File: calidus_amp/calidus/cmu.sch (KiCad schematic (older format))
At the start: 19 parts

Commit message: Daily update
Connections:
- net +pdvs: now also U?.20 (Vdd)
- net uart_rx: now also U?.18 (RC7); no longer U?.17 (RC6)
- net uart_tx: now also U?.17 (RC6); no longer U?.18 (RC7)
- net icsprst: now reaches R?.2, U?.1 (RE3/~MCLR~)
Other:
- note added: "The "pi_key_power" is tied on Vdd to \nsignal the FW boot to take instant \non action."
- note added: "pc_i2c_scl"
- note added: "pc_i2c_sda"
- note added: "pc_uart_rx"
- note added: "pc_uart_tx"
- note added: "pi_det_ac_power"
- note added: "pi_det_overload"
- note added: "pi_det_signal"
- note added: "pi_key_mute"
- note added: "pi_key_power"
- note added: "po_ctrl_enable"
- note added: "po_ctrl_mute"
- note added: "po_ctrl_pbypass"
- note added: "po_ctrl_power"
- note added: "po_ind_overload"
- note added: "po_ind_power_a"
- note added: "po_status"
- note removed: "The key "power" is tied on Vdd to \nsignal the FW boot to take instant \non action."
- moved on the sheet: D?, Q?, R?, U?

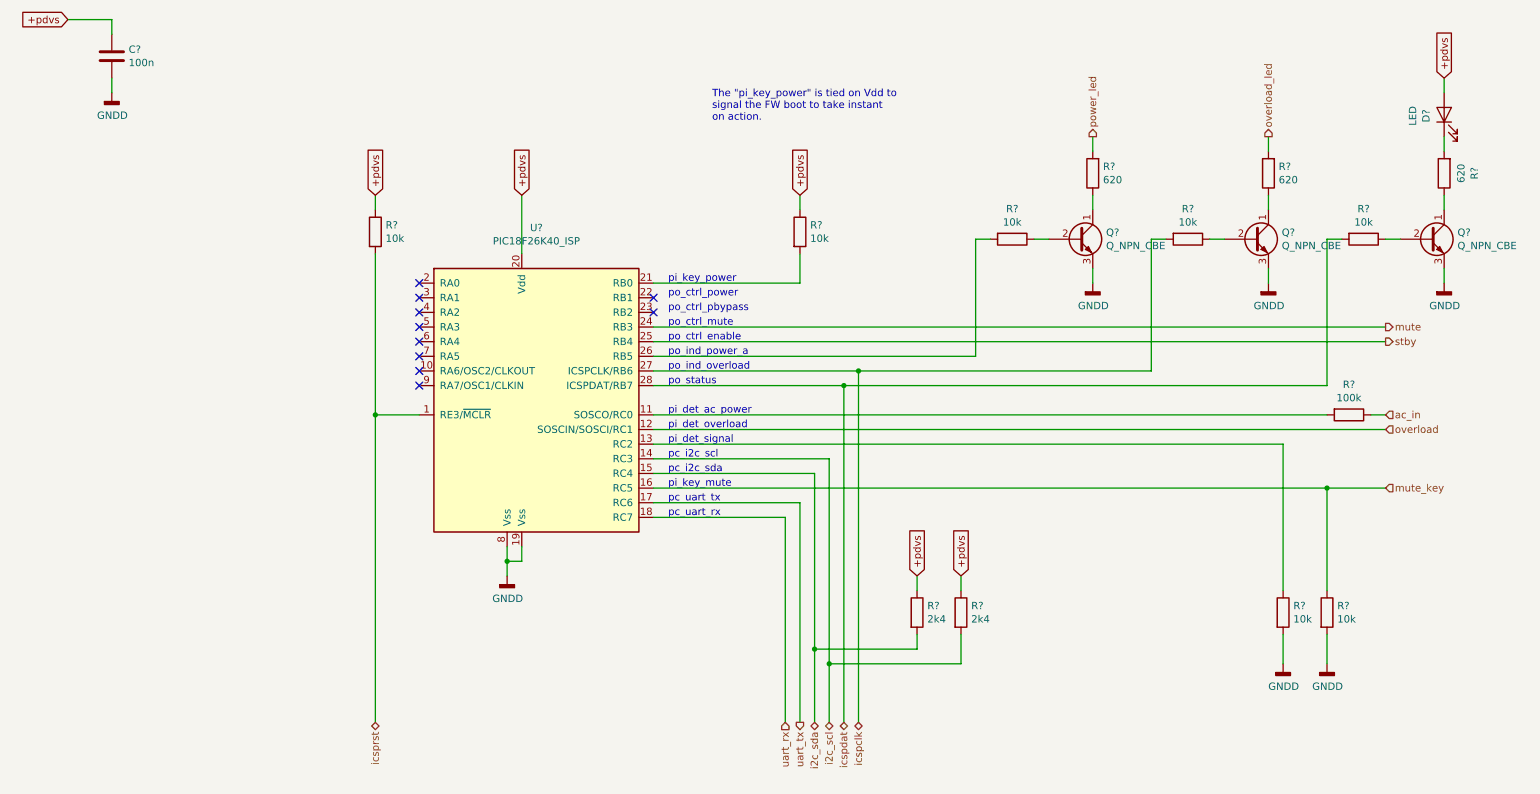
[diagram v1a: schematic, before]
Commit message: Updated component designators and finished CMU
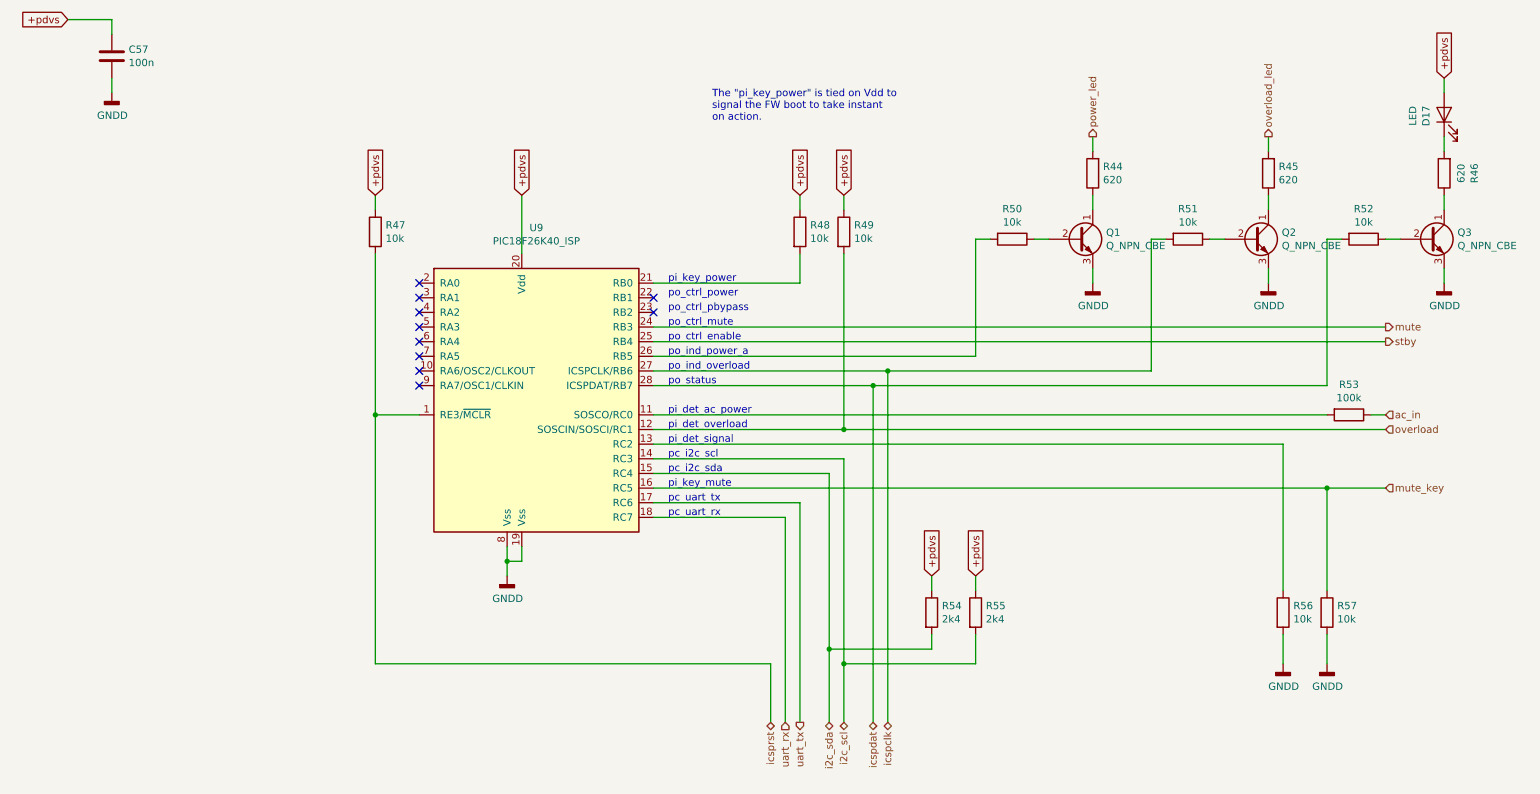
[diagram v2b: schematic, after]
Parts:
- added R49: 10k, symbol Device:R
- D17: renamed from D?; footprint (none) -> LED_THT:LED_D3.0mm
- U9: renamed from U?; footprint Package_SO:SSOP-28_5.3x10.2mm_P0.65mm -> Package_DIP:DIP-28_W7.62mm_LongPads
- gave numbers to parts that had none: 17
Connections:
- net +pdvs: now also R49.1
- net overload: now also R49.2
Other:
- moved on the sheet: R54, R55

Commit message: WIP: Updated footprints
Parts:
- removed R45, R46: 620, symbol Device:R
- removed R48, R49, R50, R51, R52, R56, R57: 10k, symbol Device:R
- removed R55: 2k4, symbol Device:R
- added C?: 10u, Capacitor_THT:CP_Radial_D5.0mm_P2.00mm, symbol Device:CP
- added R? (x7): 10k, Resistor_THT:R_Axial_DIN0204_L3.6mm_D1.6mm_P5.08mm_Horizontal, symbol Device:R
- added R?: 2k4, Resistor_THT:R_Axial_DIN0204_L3.6mm_D1.6mm_P5.08mm_Horizontal, symbol Device:R
- added R? (x2): 620, Resistor_THT:R_Axial_DIN0204_L3.6mm_D1.6mm_P5.08mm_Horizontal, symbol Device:R
- R44: footprint (none) -> Resistor_THT:R_Axial_DIN0204_L3.6mm_D1.6mm_P5.08mm_Horizontal; Manufacturer (none) -> Multicomp:MF12 620R; Power (none) -> 1/8; Supplier1 (none) -> Farnell:9343407; Type (none) -> C
- R47: footprint (none) -> Resistor_THT:R_Axial_DIN0204_L3.6mm_D1.6mm_P5.08mm_Horizontal; Manufacturer (none) -> Multicomp:MF12 10K; Power (none) -> 1/8; Supplier1 (none) -> Farnell:9342419; Type (none) -> C
- R54: footprint (none) -> Resistor_THT:R_Axial_DIN0204_L3.6mm_D1.6mm_P5.08mm_Horizontal; Manufacturer (none) -> Multicomp:MF12 2K4; Power (none) -> 1/8; Supplier1 (none) -> Farnell:9342893; Type (none) -> C
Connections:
- net +pdvs: now also C?.1, R?.1, R?.1, R?.1
- net GNDD: now also C?.2, R?.2, R?.2
- net i2c_scl: now also R?.2
- net icspclk: now also R?.2
- net icspdat: now also R?.2
- net mute_key: now also R?.1
- net overload: now also R?.2
- net overload_led: now also R?.2
- net at Q1.2 (B): now also R?.1
- net at U9.26 (RB5): now also R?.2
- net at Q2.1 (C): now also R?.1
- net at Q2.2 (B): now also R?.1
- net at Q3.1 (C): now also R?.1
- net at D17.1 (K): now also R?.2
- net at Q3.2 (B): now also R?.1
- net at U9.13 (RC2): now also R?.1
- net at U9.21 (RB0): now also R?.2

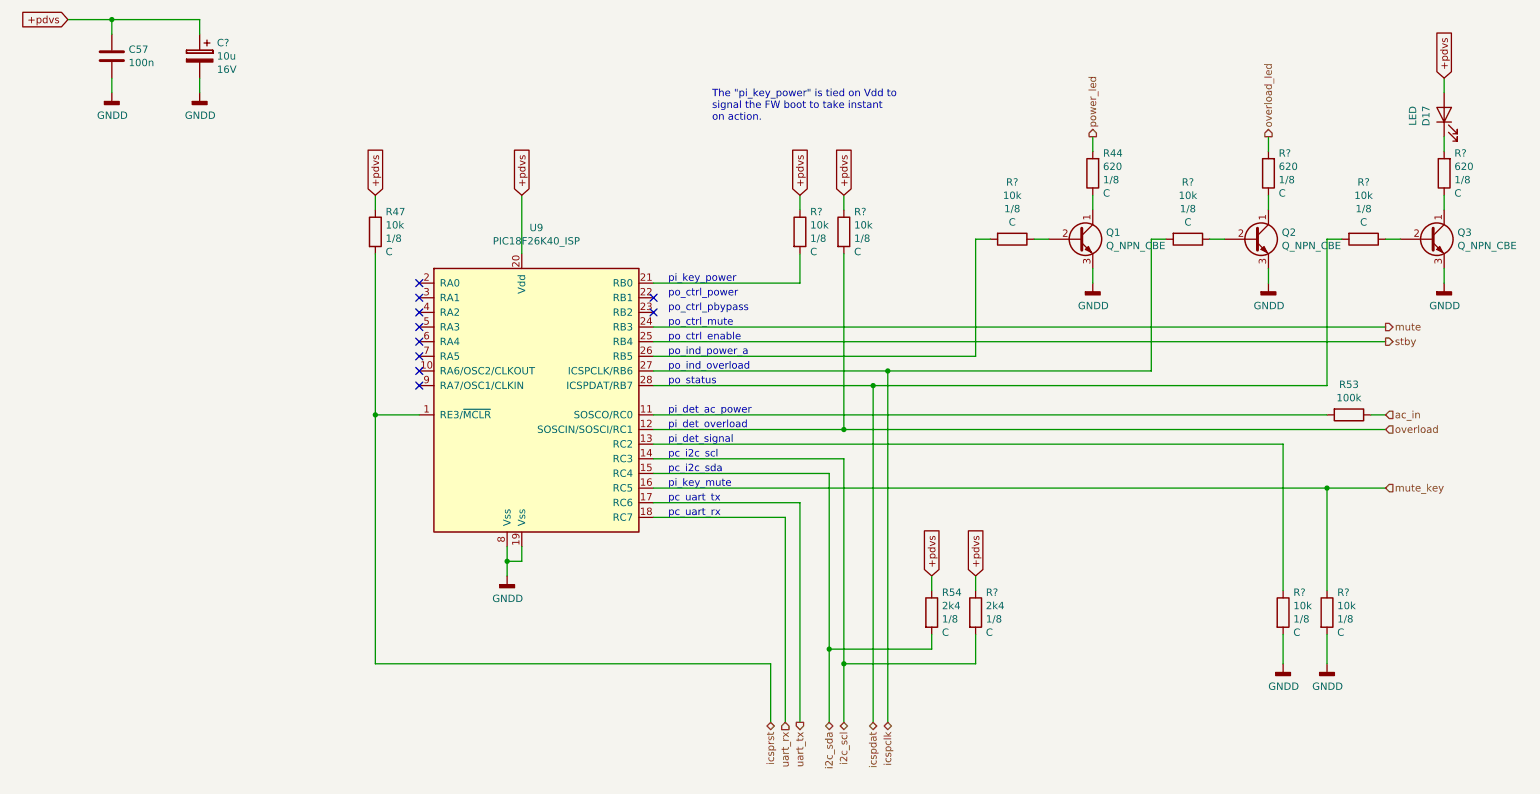
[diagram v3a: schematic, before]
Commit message: WIP: component footprint assignment.
Signed-off-by: Nenad Radulovic <nenad.b.radulovic@gmail.com>
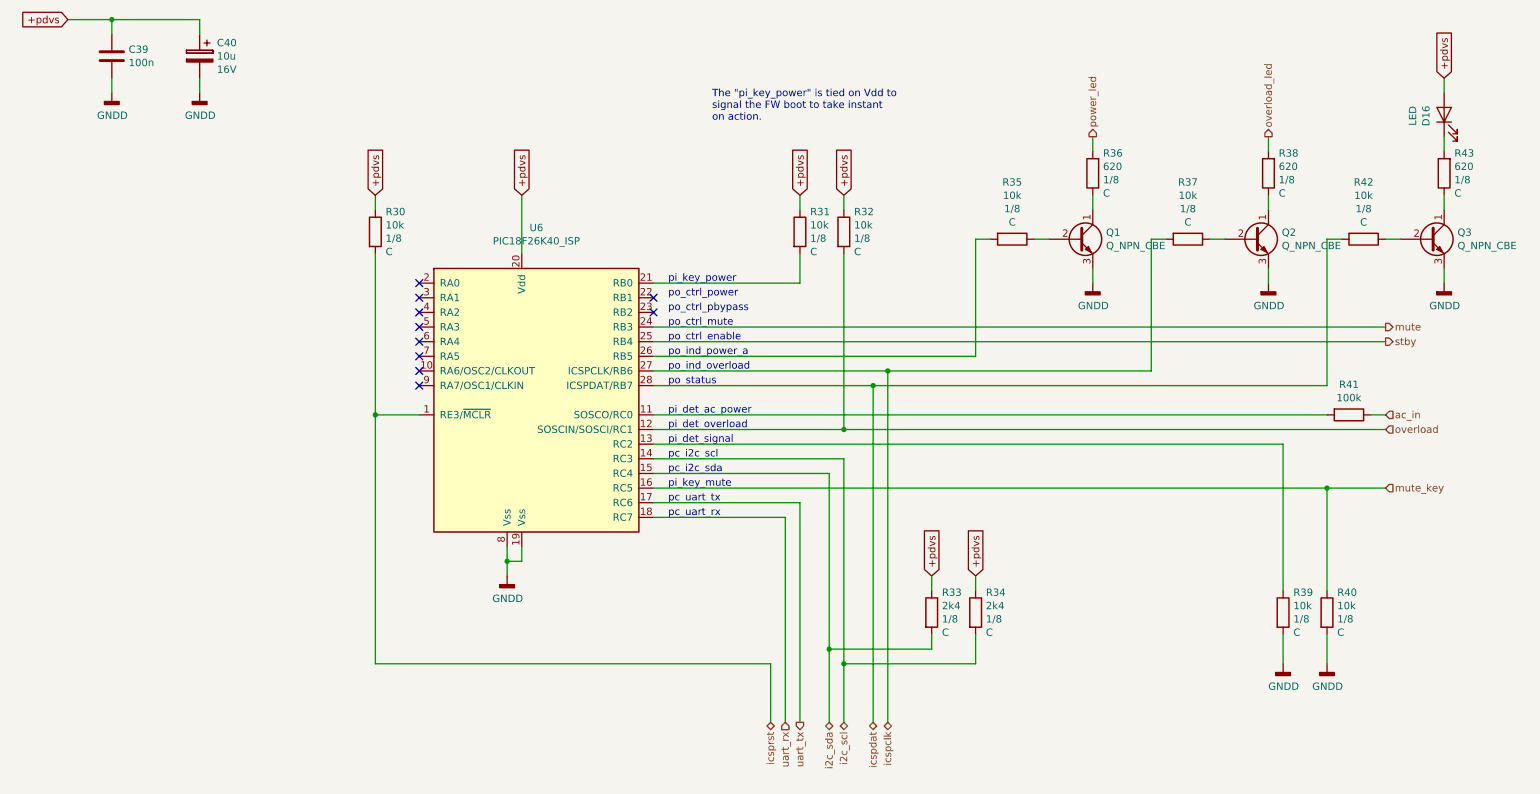
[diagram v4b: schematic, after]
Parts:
- C39: renamed from C57; footprint (none) -> Capacitor_THT:C_Rect_L7.0mm_W2.5mm_P5.00mm
- Q1, Q2, Q3: footprint (none) -> Package_TO_SOT_THT:TO-92_HandSolder
- R41: renamed from R53; footprint (none) -> Resistor_THT:R_Axial_DIN0207_L6.3mm_D2.5mm_P7.62mm_Horizontal
- gave numbers to parts that had none: 11
- renumbered D17 to D16, R47 to R30, R54 to R33, R44 to R36, U9 to U6
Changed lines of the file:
@@
 $Descr A4 11693 8268
 encoding utf-8
-Sheet 5 5
+Sheet 5 4
 Title ""
 Date ""
@@
 $EndDescr
 $Comp
-L power:GNDD #PWR036
+L power:GNDD #PWR031
 U 1 1 5C444574
 P 4200 5200
-F 0 "#PWR036" H 4200 4950 50  0001 C CNN
+F 0 "#PWR031" H 4200 4950 50  0001 C CNN
 F 1 "GNDD" H 4204 5045 50  0000 C CNN
 F 2 "" H 4200 5200 50  0001 C CNN
@@
 	1500 1400 1500 1500
 $Comp
-L power:GNDD #PWR032
+L power:GNDD #PWR029
 U 1 1 5C444792
 P 1500 1900
-F 0 "#PWR032" H 1500 1650 50  0001 C CNN
+F 0 "#PWR029" H 1500 1650 50  0001 C CNN
 F 1 "GNDD" H 1504 1745 50  0000 C CNN
 F 2 "" H 1500 1900 50  0001 C CNN
@@
 $EndComp
 $Comp
-L Device:C C57
+L Device:C C39
 U 1 1 5C46D3BF
 P 1500 1650
-F 0 "C57" H 1615 1696 50  0000 L CNN
+F 0 "C39" H 1615 1696 50  0000 L CNN
 F 1 "100n" H 1615 1605 50  0000 L CNN
-F 2 "" H 1538 1500 50  0001 C CNN
+F 2 "Capacitor_THT:C_Rect_L7.0mm_W2.5mm_P5.00mm" H 1538 1500 50  0001 C CNN
 F 3 "~" H 1500 1650 50  0001 C CNN
 	1    1500 1650
@@
 	1500 1800 1500 1900
 $Comp
-L pic18f26k40_isp:PIC18F26K40_ISP U9
+L pic18f26k40_isp:PIC18F26K40_ISP U6
 U 1 1 5C470457
 P 4400 4000
-F 0 "U9" H 4400 5178 50  0000 C CNN
+F 0 "U6" H 4400 5178 50  0000 C CNN
 F 1 "PIC18F26K40_ISP" H 4400 5087 50  0000 C CNN
 F 2 "Package_DIP:DIP-28_W7.62mm_LongPads" H 3900 3500 50  0001 C CNN
@@
 NoConn ~ 5200 3300
 $Comp
-L Device:R R44
+L Device:R R36
 U 1 1 5C48301D
 P 8200 2450
-F 0 "R44" H 8130 2313 50  0000 R CNN
+F 0 "R36" H 8130 2313 50  0000 R CNN
 F 1 "620" H 8130 2404 50  0000 R CNN
 F 2 "Resistor_THT:R_Axial_DIN0204_L3.6mm_D1.6mm_P5.08mm_Horizontal" V 8130 2450 50  0001 C CNN
@@
 overload_led
 $Comp
-L Device:LED D17
+L Device:LED D16
 U 1 1 5C4834BB
 P 10600 2050
-F 0 "D17" H 10592 2173 50  0000 C CNN
+F 0 "D16" H 10592 2173 50  0000 C CNN
 F 1 "LED" H 10592 2264 50  0000 C CNN
 F 2 "LED_THT:LED_D3.0mm" H 10600 2050 50  0001 C CNN
@@
 $EndComp
 $Comp
-L power:GNDD #PWR033
+L power:GNDD #PWR032
 U 1 1 5C4835A2
 P 8200 3200
-F 0 "#PWR033" H 8200 2950 50  0001 C CNN
+F 0 "#PWR032" H 8200 2950 50  0001 C CNN
 F 1 "GNDD" H 8204 3045 50  0000 C CNN
 F 2 "" H 8200 3200 50  0001 C CNN
@@
 F 0 "Q1" H 8291 2946 50  0000 L CNN
 F 1 "Q_NPN_CBE" H 8291 2855 50  0000 L CNN
-F 2 "" H 8300 3000 50  0001 C CNN
+F 2 "Package_TO_SOT_THT:TO-92_HandSolder" H 8300 3000 50  0001 C CNN
 F 3 "~" H 8100 2900 50  0001 C CNN
 	1    8100 2900
@@
 F 0 "Q2" H 9491 2946 50  0000 L CNN
 F 1 "Q_NPN_CBE" H 9491 2855 50  0000 L CNN
-F 2 "" H 9500 3000 50  0001 C CNN
+F 2 "Package_TO_SOT_THT:TO-92_HandSolder" H 9500 3000 50  0001 C CNN
 F 3 "~" H 9300 2900 50  0001 C CNN
 	1    9300 2900
@@
 F 0 "Q3" H 10691 2946 50  0000 L CNN
 F 1 "Q_NPN_CBE" H 10691 2855 50  0000 L CNN
-F 2 "" H 10700 3000 50  0001 C CNN
+F 2 "Package_TO_SOT_THT:TO-92_HandSolder" H 10700 3000 50  0001 C CNN
 F 3 "~" H 10500 2900 50  0001 C CNN
 	1    10500 2900
@@
 	8200 3200 8200 3100
 $Comp
-L power:GNDD #PWR034
+L power:GNDD #PWR033
 U 1 1 5C46343D
 P 9400 3200
-F 0 "#PWR034" H 9400 2950 50  0001 C CNN
+F 0 "#PWR033" H 9400 2950 50  0001 C CNN
 F 1 "GNDD" H 9404 3045 50  0000 C CNN
 F 2 "" H 9400 3200 50  0001 C CNN
@@
 $EndComp
 $Comp
-L power:GNDD #PWR035
+L power:GNDD #PWR036
 U 1 1 5C463464
 P 10600 3200
-F 0 "#PWR035" H 10600 2950 50  0001 C CNN
+F 0 "#PWR036" H 10600 2950 50  0001 C CNN
 F 1 "GNDD" H 10604 3045 50  0000 C CNN
 F 2 "" H 10600 3200 50  0001 C CNN
@@
 	9800 2900 9900 2900
 $Comp
-L Device:R R47
+L Device:R R30
 U 1 1 5C4640C2
 P 3300 2850
-F 0 "R47" H 3370 2987 50  0000 L CNN
+F 0 "R30" H 3370 2987 50  0000 L CNN
 F 1 "10k" H 3370 2896 50  0000 L CNN
 F 2 "Resistor_THT:R_Axial_DIN0204_L3.6mm_D1.6mm_P5.08mm_Horizontal" V 3230 2850 50  0001 C CNN
@@
 	10200 4200 6500 4200
 $Comp
-L Device:R R53
+L Device:R R41
 U 1 1 5C466052
 P 9950 4100
-F 0 "R53" V 9743 4100 50  0000 C CNN
+F 0 "R41" V 9743 4100 50  0000 C CNN
 F 1 "100k" V 9834 4100 50  0000 C CNN
-F 2 "" V 9880 4100 50  0001 C CNN
+F 2 "Resistor_THT:R_Axial_DIN0207_L6.3mm_D2.5mm_P7.62mm_Horizontal" V 9880 4100 50  0001 C CNN
 F 3 "~" H 9950 4100 50  0001 C CNN
 	1    9950 4100
@@
 	6500 4400 5200 4400
 $Comp
-L power:GNDD #PWR037
+L power:GNDD #PWR034
 U 1 1 5C475E16
 P 9500 5800
-F 0 "#PWR037" H 9500 5550 50  0001 C CNN
+F 0 "#PWR034" H 9500 5550 50  0001 C CNN
 F 1 "GNDD" H 9504 5645 50  0000 C CNN
 F 2 "" H 9500 5800 50  0001 C CNN
@@
 $EndComp
 $Comp
-L power:GNDD #PWR038
+L power:GNDD #PWR035
 U 1 1 5C476CD2
 P 9800 5800
-F 0 "#PWR038" H 9800 5550 50  0001 C CNN
+F 0 "#PWR035" H 9800 5550 50  0001 C CNN
 F 1 "GNDD" H 9804 5645 50  0000 C CNN
 F 2 "" H 9800 5800 50  0001 C CNN
@@
 $EndComp
 $Comp
-L Device:R R54
+L Device:R R33
 U 1 1 5C477BD2
 P 7100 5450
-F 0 "R54" H 7170 5587 50  0000 L CNN
+F 0 "R33" H 7170 5587 50  0000 L CNN
 F 1 "2k4" H 7170 5496 50  0000 L CNN
 F 2 "Resistor_THT:R_Axial_DIN0204_L3.6mm_D1.6mm_P5.08mm_Horizontal" V 7030 5450 50  0001 C CNN
@@
 	6500 4200 5200 4200
 $Comp
-L Device:R R?
+L Device:R R31
 U 1 1 5C4C2301
 P 6200 2850
-F 0 "R?" H 6270 2987 50  0000 L CNN
+F 0 "R31" H 6270 2987 50  0000 L CNN
 F 1 "10k" H 6270 2896 50  0000 L CNN
 F 2 "Resistor_THT:R_Axial_DIN0204_L3.6mm_D1.6mm_P5.08mm_Horizontal" V 6130 2850 50  0001 C CNN
@@
 $EndComp
 $Comp
-L Device:R R?
+L Device:R R32
 U 1 1 5C4C234B
 P 6500 2850
-F 0 "R?" H 6570 2987 50  0000 L CNN
+F 0 "R32" H 6570 2987 50  0000 L CNN
 F 1 "10k" H 6570 2896 50  0000 L CNN
 F 2 "Resistor_THT:R_Axial_DIN0204_L3.6mm_D1.6mm_P5.08mm_Horizontal" V 6430 2850 50  0001 C CNN
@@
 $EndComp
 $Comp
-L Device:R R?
+L Device:R R39
 U 1 1 5C4C2657
 P 9500 5450
-F 0 "R?" H 9570 5587 50  0000 L CNN
+F 0 "R39" H 9570 5587 50  0000 L CNN
 F 1 "10k" H 9570 5496 50  0000 L CNN
 F 2 "Resistor_THT:R_Axial_DIN0204_L3.6mm_D1.6mm_P5.08mm_Horizontal" V 9430 5450 50  0001 C CNN
@@
 $EndComp
 $Comp
-L Device:R R?
+L Device:R R40
 U 1 1 5C4C26B7
 P 9800 5450
-F 0 "R?" H 9870 5587 50  0000 L CNN
+F 0 "R40" H 9870 5587 50  0000 L CNN
 F 1 "10k" H 9870 5496 50  0000 L CNN
 F 2 "Resistor_THT:R_Axial_DIN0204_L3.6mm_D1.6mm_P5.08mm_Horizontal" V 9730 5450 50  0001 C CNN
@@
 $EndComp
 $Comp
-L Device:R R?
+L Device:R R35
 U 1 1 5C4C2732
 P 7650 2900
-F 0 "R?" V 7261 2900 50  0000 C CNN
+F 0 "R35" V 7261 2900 50  0000 C CNN
 F 1 "10k" V 7352 2900 50  0000 C CNN
 F 2 "Resistor_THT:R_Axial_DIN0204_L3.6mm_D1.6mm_P5.08mm_Horizontal" V 7580 2900 50  0001 C CNN
@@
 $EndComp
 $Comp
-L Device:R R?
+L Device:R R37
 U 1 1 5C4C2878
 P 8850 2900
-F 0 "R?" V 8461 2900 50  0000 C CNN
+F 0 "R37" V 8461 2900 50  0000 C CNN
 F 1 "10k" V 8552 2900 50  0000 C CNN
 F 2 "Resistor_THT:R_Axial_DIN0204_L3.6mm_D1.6mm_P5.08mm_Horizontal" V 8780 2900 50  0001 C CNN
@@
 $EndComp
 $Comp
-L Device:R R?
+L Device:R R42
 U 1 1 5C4C28CE
 P 10050 2900
-F 0 "R?" V 9661 2900 50  0000 C CNN
+F 0 "R42" V 9661 2900 50  0000 C CNN
 F 1 "10k" V 9752 2900 50  0000 C CNN
 F 2 "Resistor_THT:R_Axial_DIN0204_L3.6mm_D1.6mm_P5.08mm_Horizontal" V 9980 2900 50  0001 C CNN
@@
 P 2100 1650
 AR Path="/5C37BC7C/5C4C9FCF" Ref="C?"  Part="1"
-AR Path="/5C43C4AB/5C4C9FCF" Ref="C?"  Part="1"
-F 0 "C?" H 1982 1741 50  0000 R CNN
+AR Path="/5C43C4AB/5C4C9FCF" Ref="C40"  Part="1"
+F 0 "C40" H 1982 1741 50  0000 R CNN
 F 1 "10u" H 1982 1650 50  0000 R CNN
 F 2 "Capacitor_THT:CP_Radial_D5.0mm_P2.00mm" H 2138 1500 50  0001 C CNN
@@
 $EndComp
 $Comp
-L power:GNDD #PWR?
+L power:GNDD #PWR030
 U 1 1 5C4CB7C3
 P 2100 1900
-F 0 "#PWR?" H 2100 1650 50  0001 C CNN
+F 0 "#PWR030" H 2100 1650 50  0001 C CNN
 F 1 "GNDD" H 2104 1745 50  0000 C CNN
 F 2 "" H 2100 1900 50  0001 C CNN
@@
 Connection ~ 1500 1400
 $Comp
-L Device:R R?
+L Device:R R34
 U 1 1 5C4F79CD
 P 7400 5450
-F 0 "R?" H 7470 5587 50  0000 L CNN
+F 0 "R34" H 7470 5587 50  0000 L CNN
 F 1 "2k4" H 7470 5496 50  0000 L CNN
 F 2 "Resistor_THT:R_Axial_DIN0204_L3.6mm_D1.6mm_P5.08mm_Horizontal" V 7330 5450 50  0001 C CNN
@@
 $EndComp
 $Comp
-L Device:R R?
+L Device:R R38
 U 1 1 5C4F9272
 P 9400 2450
-F 0 "R?" H 9330 2313 50  0000 R CNN
+F 0 "R38" H 9330 2313 50  0000 R CNN
 F 1 "620" H 9330 2404 50  0000 R CNN
 F 2 "Resistor_THT:R_Axial_DIN0204_L3.6mm_D1.6mm_P5.08mm_Horizontal" V 9330 2450 50  0001 C CNN
@@
 $EndComp
 $Comp
-L Device:R R?
+L Device:R R43
 U 1 1 5C4F92B8
 P 10600 2450
-F 0 "R?" H 10530 2313 50  0000 R CNN
+F 0 "R43" H 10530 2313 50  0000 R CNN
 F 1 "620" H 10530 2404 50  0000 R CNN
 F 2 "Resistor_THT:R_Axial_DIN0204_L3.6mm_D1.6mm_P5.08mm_Horizontal" V 10530 2450 50  0001 C CNN
